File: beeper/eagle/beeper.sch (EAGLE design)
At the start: 29 parts, among them Q1 16MHz, T1 3904, U1 ATMEGA328P, U2 ATA6631

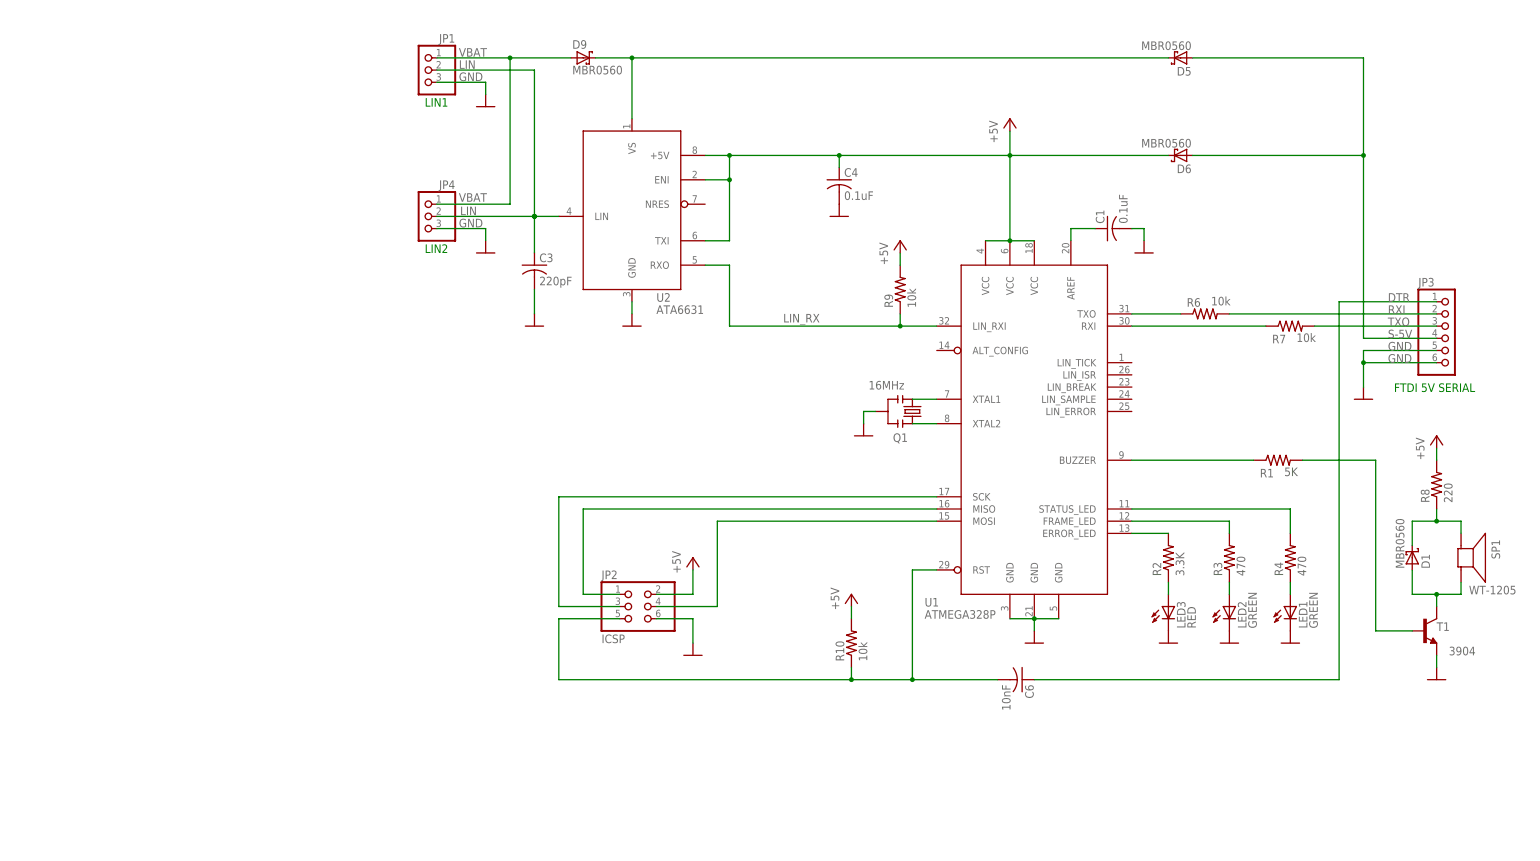
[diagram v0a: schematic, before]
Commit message: Updated the schema: added bypass caps, added fuse, minor tweaks.
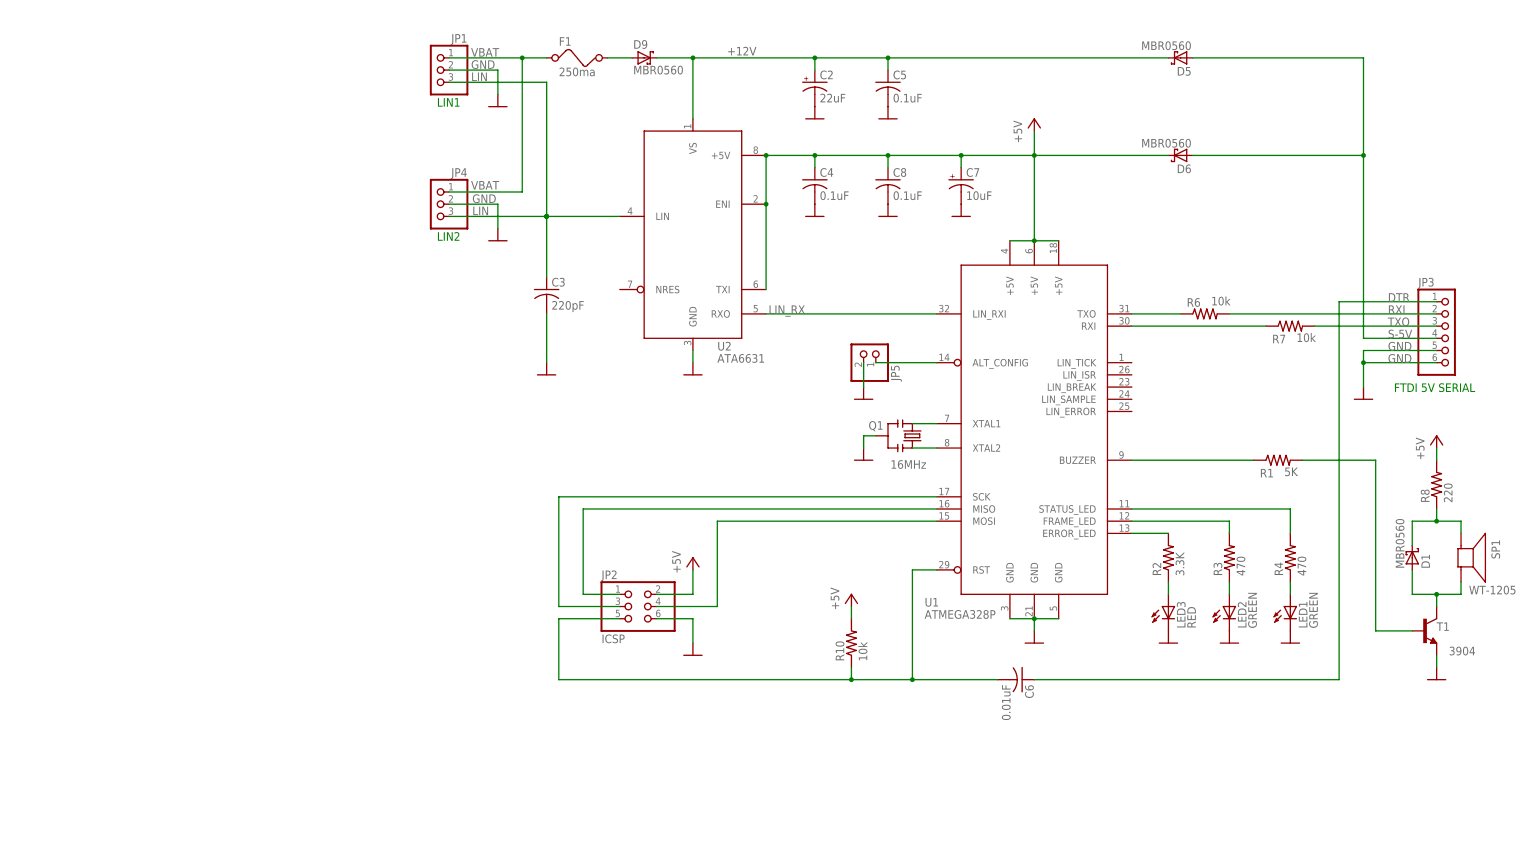
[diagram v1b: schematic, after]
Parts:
- removed C1: 0.1uF, rcl:C-USC0805
- removed R9: 10k, rcl:R-US_R0805
- added C2: 22uF, rcl:CPOL-USUD-6,3X5,8
- added C5, C8: 0.1uF, rcl:C-USC0805
- added C7: 10uF, rcl:CPOL-USA/3216-18R
- added F1: 250ma, beeper:FUSE
- added JP5: (no value), pinhead:PINHD-1X2
- C6: value 10nF -> 0.01uF
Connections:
- new net N$6: D9.A, F1.2
- net +12V: now also C2.+, C5.1
- net +5V: now also C7.+, C8.1, U1.+5V@1, U1.+5V@2, U1.+5V@3; no longer R9.2, U1.VCC@1, U1.VCC@2, U1.VCC@3
- net GND: now also C2.-, C5.2, C7.-, C8.2, JP1.2, JP4.2, JP5.2; no longer C1.2, JP1.3, JP4.3
- net LIN: now also JP1.3, JP4.3; no longer JP1.2, JP4.2
- net LIN_RX: no longer R9.1
- net N$5: now also JP5.1, U1.ALT_CONFIG; no longer C1.1, U1.AREF
- net VBAT: now also F1.1; no longer D9.A
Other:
- moved on the sheet: C3, C4, D9, JP1, JP4, Q1, U2

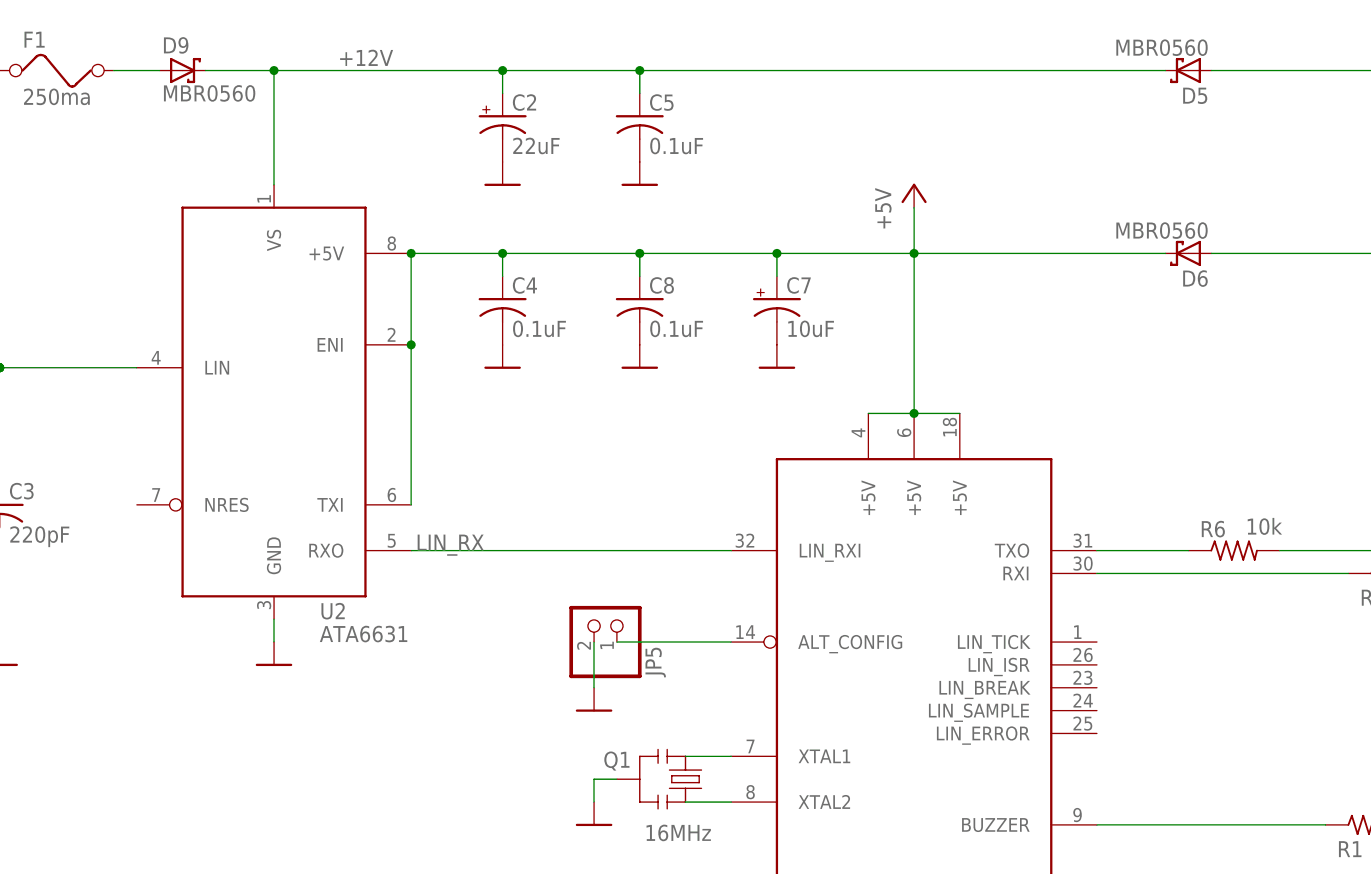
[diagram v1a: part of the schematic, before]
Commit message: Initial placement of board. Removed alt-config pin. Work in progress.
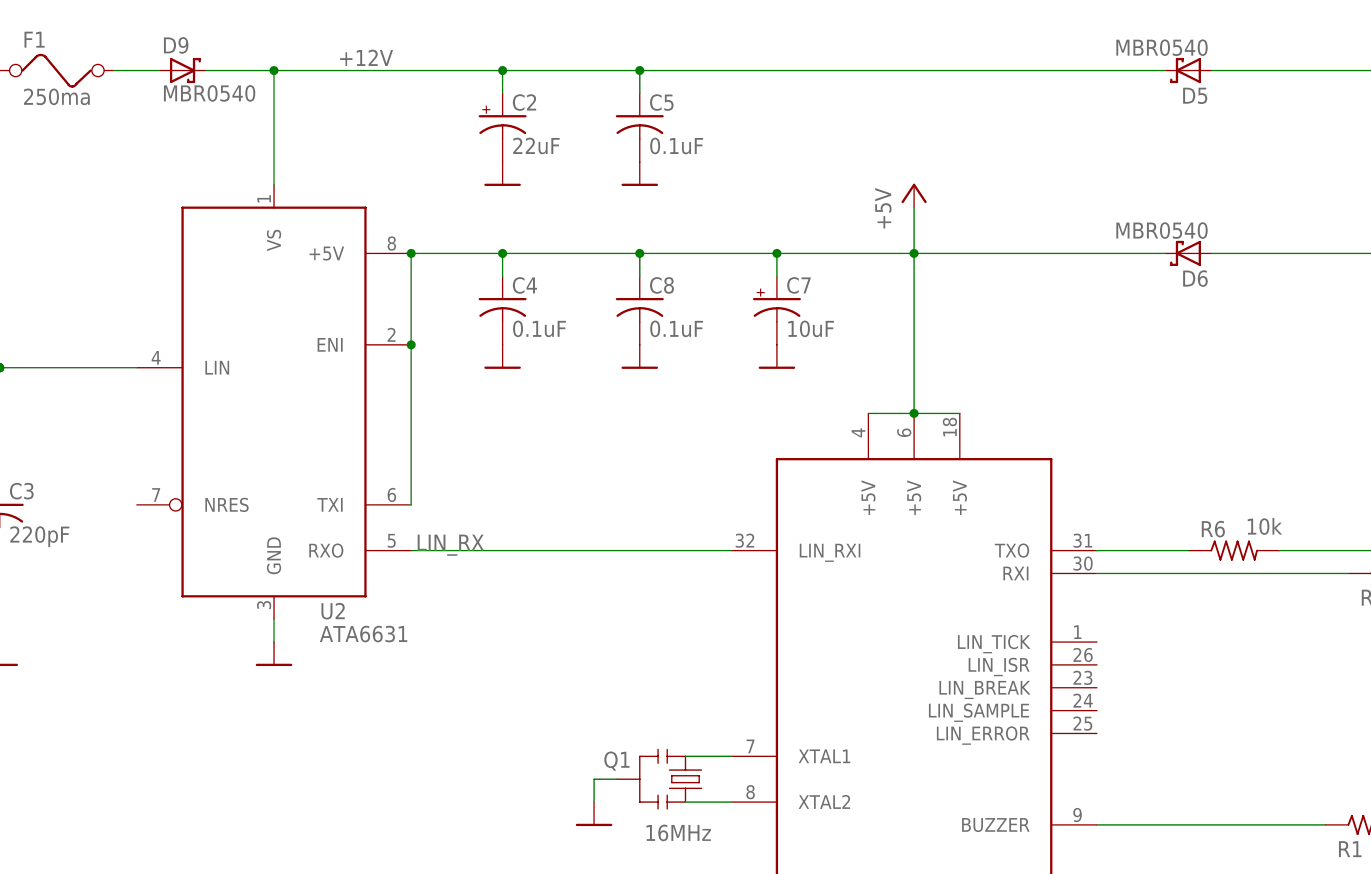
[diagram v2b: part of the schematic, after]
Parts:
- removed JP5: (no value), pinhead:PINHD-1X2
- D5, D6, D9: value MBR0560 -> MBR0540
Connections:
- removed net N$5: JP5.1, U1.ALT_CONFIG
- net GND: no longer JP5.2
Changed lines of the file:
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@@
 <part name="JP4" library="pinhead" deviceset="PINHD-1X3" device=""/>
 <part name="GND1" library="beeper" deviceset="GND" device=""/>
-<part name="D9" library="diode" deviceset="SMF5.0AT1" device="" value="MBR0560"/>
+<part name="D9" library="diode" deviceset="SMF5.0AT1" device="" value="MBR0540"/>
 <part name="U1" library="beeper" deviceset="ATMEGA328P" device=""/>
-<part name="D5" library="diode" deviceset="SMF5.0AT1" device="" value="MBR0560"/>
-<part name="D6" library="diode" deviceset="SMF5.0AT1" device="" value="MBR0560"/>
+<part name="D5" library="diode" deviceset="SMF5.0AT1" device="" value="MBR0540"/>
+<part name="D6" library="diode" deviceset="SMF5.0AT1" device="" value="MBR0540"/>
 <part name="Q1" library="SparkFun" deviceset="RESONATOR" device="SMD" value="16MHz"/>
 <part name="GND8" library="beeper" deviceset="GND" device=""/>
@@
 <part name="GND15" library="beeper" deviceset="GND" device=""/>
 <part name="GND17" library="beeper" deviceset="GND" device=""/>
-<part name="JP5" library="pinhead" deviceset="PINHD-1X2" device=""/>
-<part name="GND4" library="beeper" deviceset="GND" device=""/>
 <part name="GND11" library="beeper" deviceset="GND" device=""/>
 <part name="F1" library="beeper" deviceset="FUSE" device="" value="250ma"/>
@@
 <instance part="GND15" gate="1" x="154.94" y="187.96"/>
 <instance part="GND17" gate="1" x="170.18" y="187.96"/>
-<instance part="JP5" gate="G$1" x="165.1" y="139.7" rot="MR90"/>
-<instance part="GND4" gate="1" x="165.1" y="129.54"/>
 <instance part="GND11" gate="1" x="129.54" y="134.62"/>
 <instance part="F1" gate="G$1" x="106.68" y="200.66"/>
@@
 <pinref part="C5" gate="G$1" pin="2"/>
 <pinref part="GND17" gate="1" pin="GND"/>
-</segment>
-<segment>
-<pinref part="JP5" gate="G$1" pin="2"/>
-<wire x1="165.1" y1="137.16" x2="165.1" y2="132.08" width="0.1524" layer="91"/>
-<pinref part="GND4" gate="1" pin="GND"/>
 </segment>
 <segment>
@@
 </segment>
 </net>
-<net name="N$5" class="0">
-<segment>
-<pinref part="JP5" gate="G$1" pin="1"/>
-<pinref part="U1" gate="G$1" pin="ALT_CONFIG"/>
-<wire x1="167.64" y1="137.16" x2="180.34" y2="137.16" width="0.1524" layer="91"/>
-</segment>
-</net>

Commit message: Minor board tweaks. Work in progress.
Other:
- moved on the sheet: Q1
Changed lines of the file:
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@@
 <instance part="D5" gate="G$1" x="231.14" y="200.66" rot="R180"/>
 <instance part="D6" gate="G$1" x="231.14" y="180.34" rot="R180"/>
-<instance part="Q1" gate="G$1" x="175.26" y="121.92" smashed="yes" rot="MR90">
-<attribute name="NAME" x="166.116" y="124.968" size="1.778" layer="95" rot="MR180"/>
-<attribute name="VALUE" x="170.688" y="116.84" size="1.778" layer="96" rot="MR180"/>
+<instance part="Q1" gate="G$1" x="177.8" y="129.54" smashed="yes" rot="MR90">
+<attribute name="NAME" x="168.656" y="132.588" size="1.778" layer="95" rot="MR180"/>
+<attribute name="VALUE" x="173.228" y="124.46" size="1.778" layer="96" rot="MR180"/>
 </instance>
-<instance part="GND8" gate="1" x="165.1" y="116.84"/>
+<instance part="GND8" gate="1" x="167.64" y="124.46"/>
 <instance part="SP1" gate="G$1" x="289.56" y="96.52" smashed="yes" rot="R270">
 <attribute name="NAME" x="295.91" y="100.33" size="1.778" layer="95" rot="R270"/>
@@
 <segment>
 <pinref part="Q1" gate="G$1" pin="2"/>
-<wire x1="167.64" y1="121.92" x2="165.1" y2="121.92" width="0.1524" layer="91"/>
+<wire x1="170.18" y1="129.54" x2="167.64" y2="129.54" width="0.1524" layer="91"/>
 <pinref part="GND8" gate="1" pin="GND"/>
-<wire x1="165.1" y1="121.92" x2="165.1" y2="119.38" width="0.1524" layer="91"/>
+<wire x1="167.64" y1="129.54" x2="167.64" y2="127" width="0.1524" layer="91"/>
 </segment>
 <segment>
@@
 <pinref part="U1" gate="G$1" pin="XTAL1"/>
 <pinref part="Q1" gate="G$1" pin="3"/>
-<wire x1="180.34" y1="124.46" x2="175.26" y2="124.46" width="0.1524" layer="91"/>
+<wire x1="180.34" y1="132.08" x2="177.8" y2="132.08" width="0.1524" layer="91"/>
 </segment>
 </net>
@@
 <pinref part="Q1" gate="G$1" pin="1"/>
 <pinref part="U1" gate="G$1" pin="XTAL2"/>
-<wire x1="175.26" y1="119.38" x2="180.34" y2="119.38" width="0.1524" layer="91"/>
-</segment>
-</net>
+<wire x1="177.8" y1="127" x2="180.34" y2="127" width="0.1524" layer="91"/>
+</segment>
+</net>
